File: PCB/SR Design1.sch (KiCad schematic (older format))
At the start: 5 parts, among them J1 IMU (I2C), J2 GPS (UART), J3 BT (UART), J4 SD (SPI)

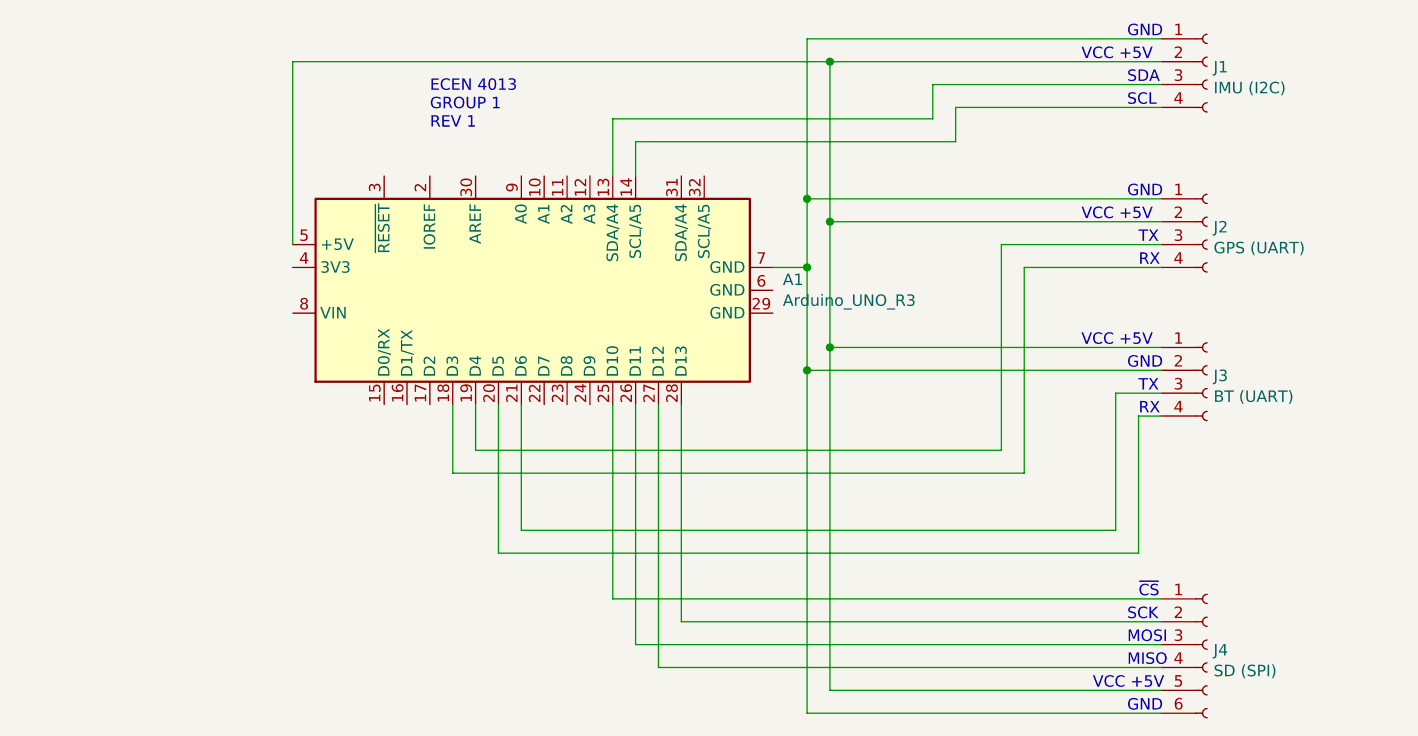
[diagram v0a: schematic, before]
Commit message: Updated PCB to REV 0.3
Updated all PCB files previously added. These should be updated to Rev 0.3 with new BT module and alternative power circuit. Board size not changed.
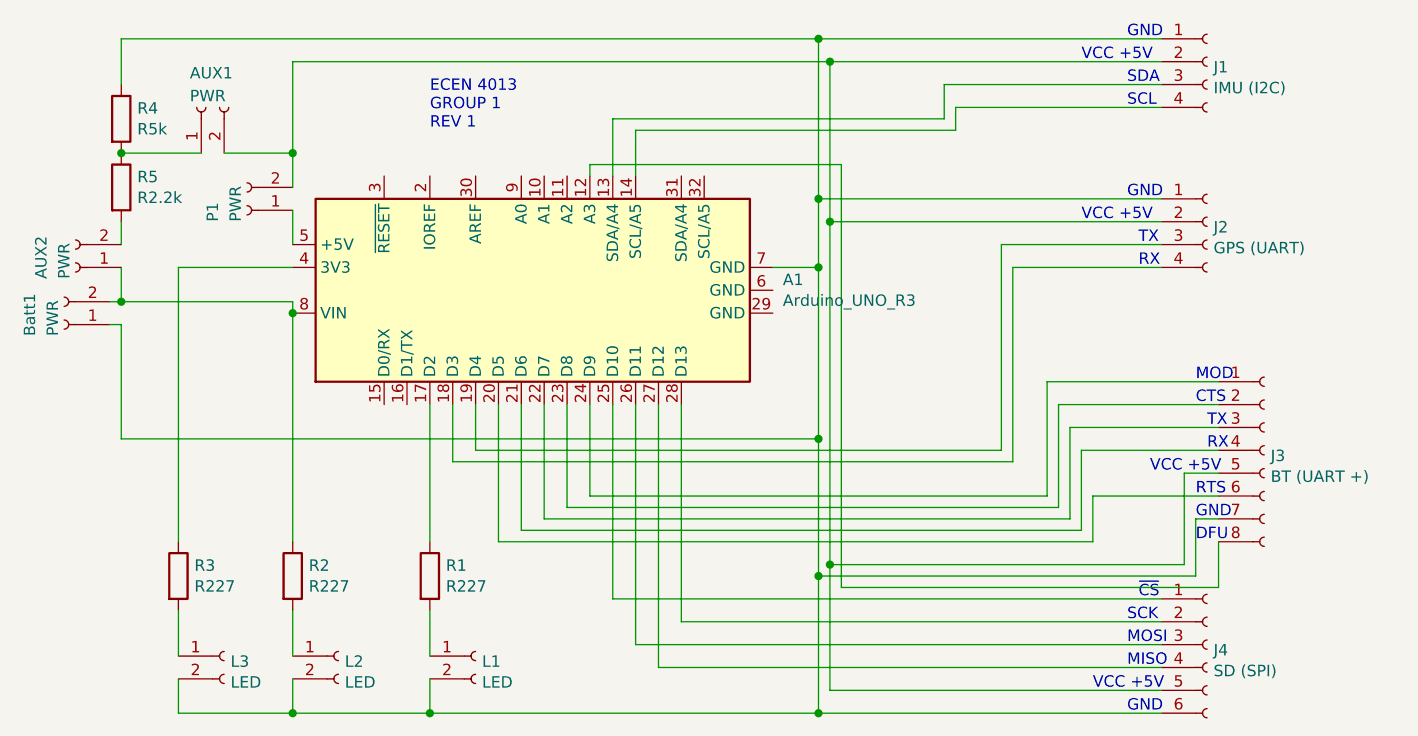
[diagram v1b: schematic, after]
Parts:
- removed J3: BT (UART), Connector_PinSocket_2.54mm:PinSocket_1x04_P2.54mm_Horizontal, symbol Connector:Conn_01x04_Female
- added AUX1, AUX2, P1: PWR, Connector_Wire:SolderWire-0.1sqmm_1x02_P3.6mm_D0.4mm_OD1mm, symbol Connector:Conn_01x02_Female
- added Batt1: PWR, Connector_JST:JST_XH_B2B-XH-A_1x02_P2.50mm_Vertical, symbol Connector:Conn_01x02_Female
- added J3: BT (UART +), Connector_PinSocket_2.54mm:PinSocket_1x08_P2.54mm_Vertical, symbol Connector:Conn_01x08_Female
- added L1, L2, L3: LED, Connector_Wire:SolderWire-0.1sqmm_1x02_P3.6mm_D0.4mm_OD1mm, symbol Connector:Conn_01x02_Female
- added R1, R2, R3: R227, Resistor_THT:R_Axial_DIN0207_L6.3mm_D2.5mm_P10.16mm_Horizontal, symbol Device:R
- added R4: R5k, Resistor_THT:R_Axial_DIN0207_L6.3mm_D2.5mm_P10.16mm_Horizontal, symbol Device:R
- added R5: R2.2k, Resistor_THT:R_Axial_DIN0207_L6.3mm_D2.5mm_P10.16mm_Horizontal, symbol Device:R
- J1, J2: footprint Connector_PinHeader_1.00mm:PinHeader_1x04_P1.00mm_Horizontal -> Connector_PinHeader_2.00mm:PinHeader_1x04_P2.00mm_Horizontal
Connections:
- net at A1.12 (A3): now also J3.8 (Pin_8)
- net at A1.17 (D2): now also R1.1
- net at A1.20 (D5): now also J3.6 (Pin_6)
- net at A1.21 (D6): now also J3.4 (Pin_4)
- net at A1.22 (D7): now also J3.3 (Pin_3)
- net at A1.23 (D8): now also J3.2 (Pin_2)
- net at A1.24 (D9): now also J3.1 (Pin_1)
- net at A1.4 (3V3): now also R3.1
- net at J1.2 (Pin_2), J2.2 (Pin_2), J4.5 (Pin_5): now also AUX1.2 (Pin_2), J3.5 (Pin_5), P1.2 (Pin_2); no longer A1.5 (+5V)
- net at A1.7 (GND), J1.1 (Pin_1), J2.1 (Pin_1)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: now also Batt1.1 (Pin_1), J3.7 (Pin_7), L1.2 (Pin_2), L2.2 (Pin_2), L3.2 (Pin_2), R4.1
- net at A1.8 (VIN): now also AUX2.1 (Pin_1), Batt1.2 (Pin_2), R2.1
- new net: A1.5 (+5V), P1.1 (Pin_1)
- new net: L1.1 (Pin_1), R1.2
- new net: L2.1 (Pin_1), R2.2
- new net: AUX1.1 (Pin_1), R4.2, R5.1
- new net: AUX2.2 (Pin_2), R5.2
- new net: L3.1 (Pin_1), R3.2
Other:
- note added: "CTS"
- note added: "DFU\n"
- note added: "MOD"
- note added: "RTS"
- note added: "TX"

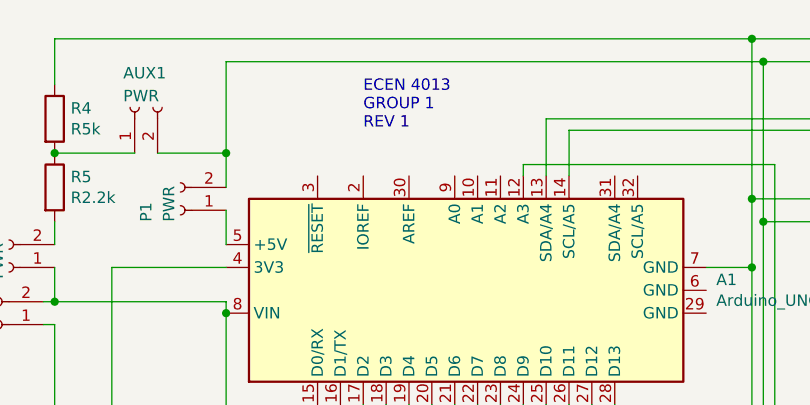
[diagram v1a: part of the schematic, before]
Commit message: Updated Schmatic
Updated Schematic to the correct revision.
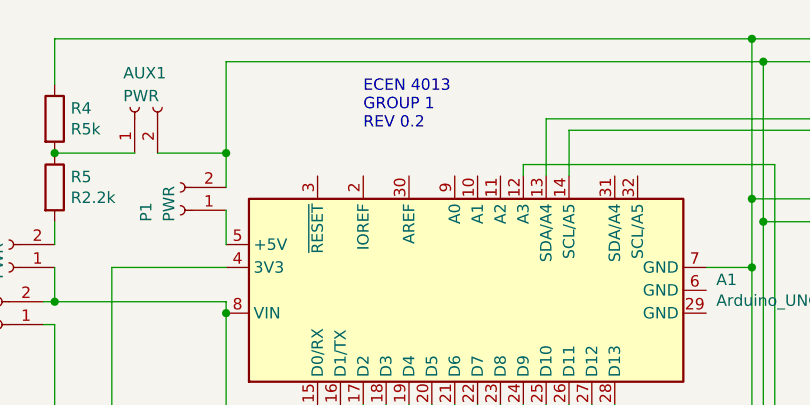
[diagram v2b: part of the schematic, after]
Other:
- note added: "ECEN 4013 \nGROUP 1\nREV 0.2\n"
- note removed: "ECEN 4013 \nGROUP 1\nREV 1\n"
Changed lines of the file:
@@
 ~CS
 Text Notes 2750 2400 0    50   ~ 0
-ECEN 4013 \nGROUP 1\nREV 1\n
+ECEN 4013 \nGROUP 1\nREV 0.2\n
 $Comp
 L Connector:Conn_01x04_Female J1
